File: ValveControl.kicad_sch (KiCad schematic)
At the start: 30 parts, among them J10 Valve_1_PWR, J11 Valve_1_PWR, J6 Valve_1_PWR, J7 Valve_1_PWR, J8 Valve_1_PWR, J9 Valve_1_PWR, Q1 BSS138, Q2 BSS138, Q3 BSS138, Q4 BSS138, Q5 BSS138, Q6 BSS138

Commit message: Add SAFE +24V
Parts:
- D3, D4, D5, D6, D7, D8: footprint (none) -> Diode_SMD:D_SMB
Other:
- title: (none) -> Valve Control
- moved on the sheet: D4, D5, D6, D7, D8, J10, J11, J6, J7, J8, J9, Q1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

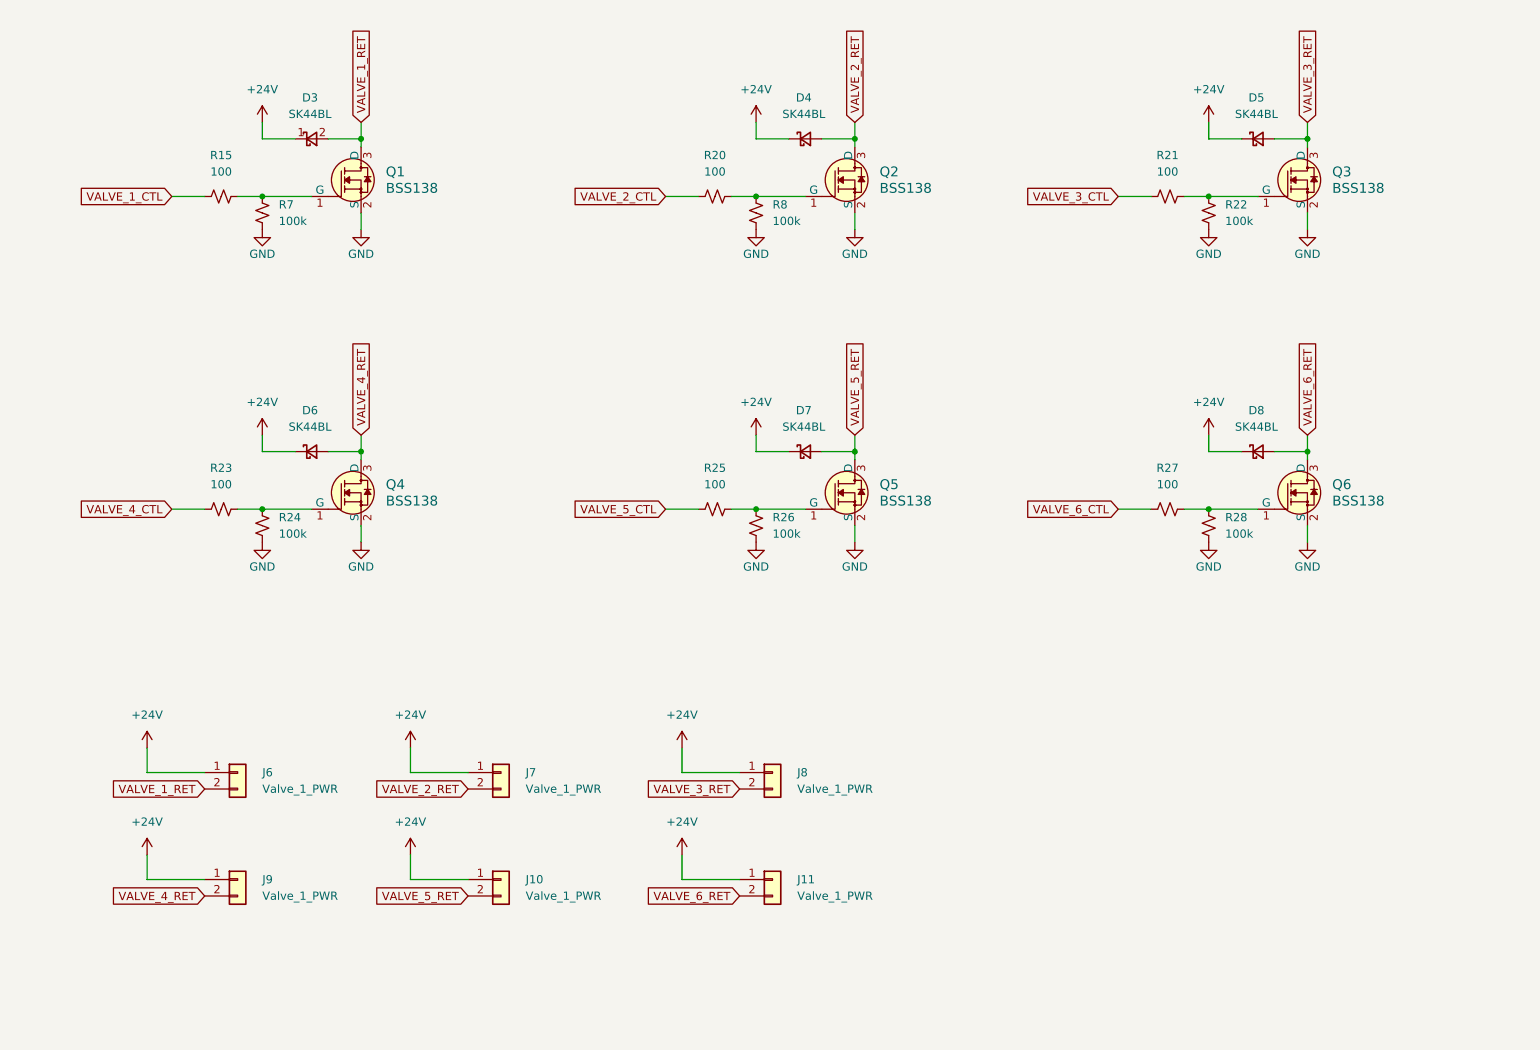
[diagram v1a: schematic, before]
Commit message: Add load cell inputs
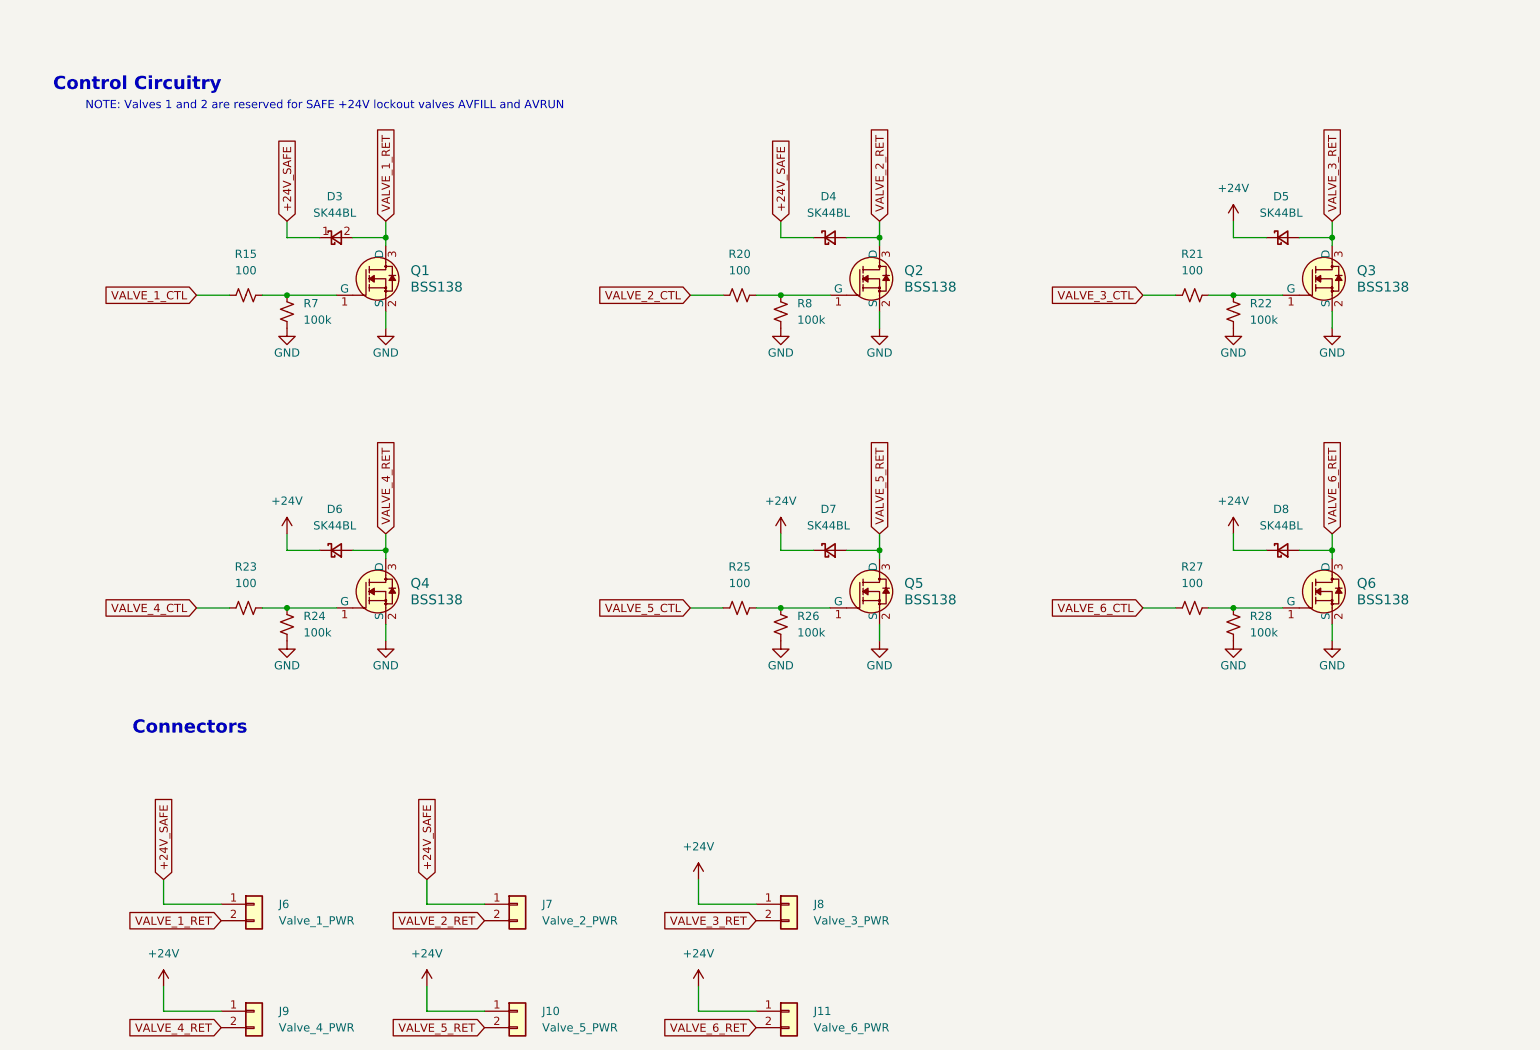
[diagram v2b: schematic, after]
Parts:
- J10: value Valve_1_PWR -> Valve_5_PWR
- J11: value Valve_1_PWR -> Valve_6_PWR
- J7: value Valve_1_PWR -> Valve_2_PWR
- J8: value Valve_1_PWR -> Valve_3_PWR
- J9: value Valve_1_PWR -> Valve_4_PWR
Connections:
- net +24V: no longer D3.1 (K), D4.1 (K), J6.1 (Pin_1), J7.1 (Pin_1)
- new net +24V_SAFE: D3.1 (K), D4.1 (K), J6.1 (Pin_1), J7.1 (Pin_1)
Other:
- note added: "Connectors"
- note added: "Control Circuitry"
- note added: "NOTE: Valves 1 and 2 are reserved for SAFE +24V lockout valves AVFILL and AVRUN"
- moved on the sheet: D3, D4, D5, D6, D7, D8, J10, J11, J6, J7, J8, J9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

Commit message: routing broken
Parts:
- renumbered D3 to D1, D6 to D2, D4 to D3, D7 to D4, D8 to D6, J6 to J3, J9 to J4, J7 to J5, J10 to J6, J8 to J7, J11 to J8, Q4 to Q2, Q2 to Q3, Q5 to Q4, Q3 to Q5, R26 to R10, R21 to R11, R27 to R12, R22 to R13, R28 to R14, R15 to R3, R23 to R4, R7 to R5, R24 to R6, R20 to R7, R25 to R8, R8 to R9

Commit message: Fix connector references
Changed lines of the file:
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@@
 		(fields_autoplaced yes)
 		(property "Reference" "J7"
-			(at 137.16 152.3999 0)
+			(at 135.89 152.3999 0)
 			(effects
 				(font
@@
 		)
 		(property "Value" "Valve_3_PWR"
-			(at 137.16 154.9399 0)
+			(at 135.89 154.9399 0)
 			(effects
 				(font

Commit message: Fix silk screening
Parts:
- J3, J4, J5, J6, J7, J8: now left out of the parts list
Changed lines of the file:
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@@
 	(title_block
 		(title "Valve Control")
-		(rev "0.1.0")
+		(rev "1.0.0")
 		(company "Queen's Rocket Engineering Team")
 	)
@@
 		(unit 1)
 		(exclude_from_sim no)
-		(in_bom yes)
+		(in_bom no)
 		(on_board yes)
 		(dnp no)
@@
 		(unit 1)
 		(exclude_from_sim no)
-		(in_bom yes)
+		(in_bom no)
 		(on_board yes)
 		(dnp no)
@@
 		(unit 1)
 		(exclude_from_sim no)
-		(in_bom yes)
+		(in_bom no)
 		(on_board yes)
 		(dnp no)
@@
 		(unit 1)
 		(exclude_from_sim no)
-		(in_bom yes)
+		(in_bom no)
 		(on_board yes)
 		(dnp no)
@@
 		(unit 1)
 		(exclude_from_sim no)
-		(in_bom yes)
+		(in_bom no)
 		(on_board yes)
 		(dnp no)
@@
 		(unit 1)
 		(exclude_from_sim no)
-		(in_bom yes)
+		(in_bom no)
 		(on_board yes)
 		(dnp no)

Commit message: connected to GPIO pins
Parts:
- renumbered D1 to D2, D2 to D3, D3 to D4, D4 to D5, D5 to D6, D6 to D7, J3 to J4, J4 to J5, J5 to J6, J6 to J7, J7 to J8, J8 to J9, R3 to R10, R4 to R11, R5 to R12, R6 to R13, R7 to R14, R8 to R15, R9 to R16, R10 to R17, R11 to R18, R12 to R19, R13 to R20, R14 to R21

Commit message: pcb first draft, changed esp32 pin connections
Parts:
- renumbered R11 to R10, R12 to R11, R13 to R12, R14 to R13, R15 to R14, R16 to R15, R17 to R16, R18 to R17, R19 to R18, R20 to R19, R21 to R20, R10 to R9
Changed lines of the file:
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@@
 		(dnp no)
 		(fields_autoplaced yes)
-		(property "Reference" "R13"
+		(property "Reference" "R12"
 			(at 58.42 107.9499 0)
 			(effects
@@
 			(project "nexus"
 				(path "/226c5870-4123-4efa-a2b3-b42d02f59bb7/5ec173b3-a2a2-49a7-aaa2-51911ea3ebad"
-					(reference "R13")
+					(reference "R12")
 					(unit 1)
 				)
@@
 		(dnp no)
 		(fields_autoplaced yes)
-		(property "Reference" "R18"
+		(property "Reference" "R17"
 			(at 195.58 52.07 90)
 			(effects
@@
 			(project "nexus"
 				(path "/226c5870-4123-4efa-a2b3-b42d02f59bb7/5ec173b3-a2a2-49a7-aaa2-51911ea3ebad"
-					(reference "R18")
+					(reference "R17")
 					(unit 1)
 				)
@@
 		(dnp no)
 		(fields_autoplaced yes)
-		(property "Reference" "R10"
+		(property "Reference" "R9"
 			(at 49.53 52.07 90)
 			(effects
@@
 			(project ""
 				(path "/226c5870-4123-4efa-a2b3-b42d02f59bb7/5ec173b3-a2a2-49a7-aaa2-51911ea3ebad"
-					(reference "R10")
+					(reference "R9")
 					(unit 1)
 				)
@@
 		(dnp no)
 		(fields_autoplaced yes)
-		(property "Reference" "R17"
+		(property "Reference" "R16"
 			(at 134.62 107.9499 0)
 			(effects
@@
 			(project "nexus"
 				(path "/226c5870-4123-4efa-a2b3-b42d02f59bb7/5ec173b3-a2a2-49a7-aaa2-51911ea3ebad"
-					(reference "R17")
+					(reference "R16")
 					(unit 1)
 				)
@@
 		(dnp no)
 		(fields_autoplaced yes)
-		(property "Reference" "R19"
+		(property "Reference" "R18"
 			(at 195.58 100.33 90)
 			(effects
@@
 			(project "nexus"
 				(path "/226c5870-4123-4efa-a2b3-b42d02f59bb7/5ec173b3-a2a2-49a7-aaa2-51911ea3ebad"
-					(reference "R19")
+					(reference "R18")
 					(unit 1)
 				)
@@
 		(dnp no)
 		(fields_autoplaced yes)
-		(property "Reference" "R16"
+		(property "Reference" "R15"
 			(at 134.62 59.6899 0)
 			(effects
@@
 			(project "nexus"
 				(path "/226c5870-4123-4efa-a2b3-b42d02f59bb7/5ec173b3-a2a2-49a7-aaa2-51911ea3ebad"
-					(reference "R16")
+					(reference "R15")
 					(unit 1)
 				)
@@
 		(dnp no)
 		(fields_autoplaced yes)
-		(property "Reference" "R20"
+		(property "Reference" "R19"
 			(at 204.47 59.6899 0)
 			(effects
@@
 			(project "nexus"
 				(path "/226c5870-4123-4efa-a2b3-b42d02f59bb7/5ec173b3-a2a2-49a7-aaa2-51911ea3ebad"
-					(reference "R20")
+					(reference "R19")
 					(unit 1)
 				)
@@
 		(dnp no)
 		(fields_autoplaced yes)
-		(property "Reference" "R21"
+		(property "Reference" "R20"
 			(at 204.47 107.9499 0)
 			(effects
@@
 			(project "nexus"
 				(path "/226c5870-4123-4efa-a2b3-b42d02f59bb7/5ec173b3-a2a2-49a7-aaa2-51911ea3ebad"
-					(reference "R21")
+					(reference "R20")
 					(unit 1)
 				)
@@
 		(dnp no)
 		(fields_autoplaced yes)
-		(property "Reference" "R11"
+		(property "Reference" "R10"
 			(at 49.53 100.33 90)
 			(effects
@@
 			(project "nexus"
 				(path "/226c5870-4123-4efa-a2b3-b42d02f59bb7/5ec173b3-a2a2-49a7-aaa2-51911ea3ebad"
-					(reference "R11")
+					(reference "R10")
 					(unit 1)
 				)
@@
 		(dnp no)
 		(fields_autoplaced yes)
-		(property "Reference" "R15"
+		(property "Reference" "R14"
 			(at 125.73 100.33 90)
 			(effects
@@
 			(project "nexus"
 				(path "/226c5870-4123-4efa-a2b3-b42d02f59bb7/5ec173b3-a2a2-49a7-aaa2-51911ea3ebad"
-					(reference "R15")
+					(reference "R14")
 					(unit 1)
 				)
@@
 		(dnp no)
 		(fields_autoplaced yes)
-		(property "Reference" "R12"
+		(property "Reference" "R11"
 			(at 58.42 59.6899 0)
 			(effects
@@
 			(project ""
 				(path "/226c5870-4123-4efa-a2b3-b42d02f59bb7/5ec173b3-a2a2-49a7-aaa2-51911ea3ebad"
-					(reference "R12")
+					(reference "R11")
 					(unit 1)
 				)
@@
 		(dnp no)
 		(fields_autoplaced yes)
-		(property "Reference" "R14"
+		(property "Reference" "R13"
 			(at 125.73 52.07 90)
 			(effects
@@
 			(project "nexus"
 				(path "/226c5870-4123-4efa-a2b3-b42d02f59bb7/5ec173b3-a2a2-49a7-aaa2-51911ea3ebad"
-					(reference "R14")
+					(reference "R13")
 					(unit 1)
 				)
